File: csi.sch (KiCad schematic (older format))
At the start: 35 parts, among them J6 WE_68715014522, J7 WE_68715014022, U4 PCA9547BS,118

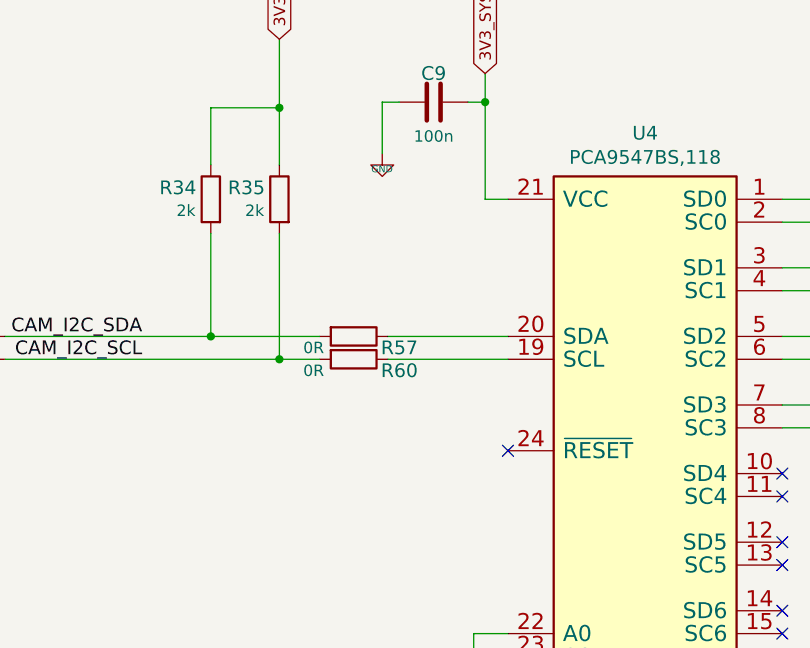
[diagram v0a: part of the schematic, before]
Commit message: Add i2c-mux reset pull-up
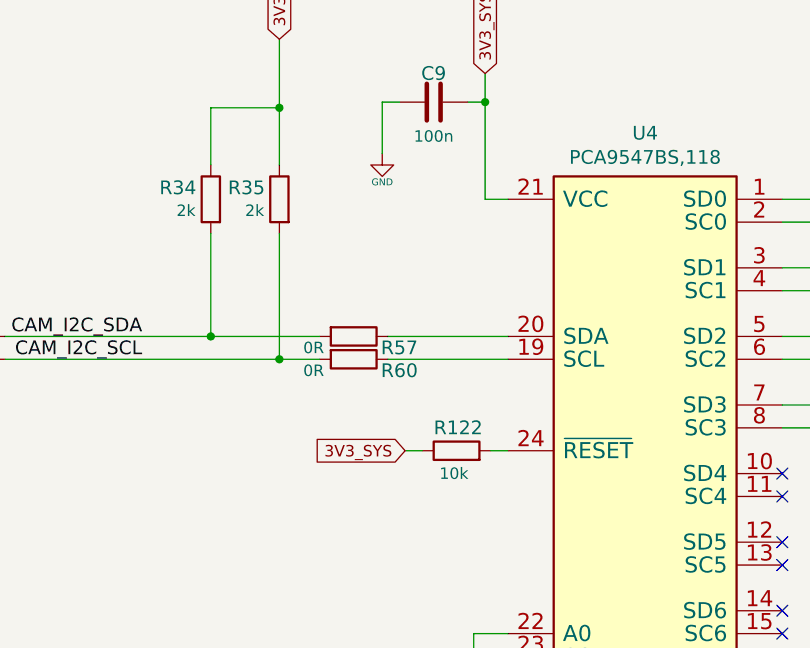
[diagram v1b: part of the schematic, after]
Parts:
- added R122: R_10k_0402, jetson-nano-baseboard-footprints:0402-res, symbol jetson-nano-baseboard:R_10k_0402
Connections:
- net 3V3_SYS: now also R122.1
- net at U4.24 (~RESET): now also R122.2
- no-connect marks 43 -> 42
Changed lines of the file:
@@
 AR Path="/60A05943/5E710510" Ref="#GND_?"  Part="1"
 F 0 "#GND_04" H 7300 8025 20  0001 C CNN
-F 1 "GND" H 7301 7957 30  0000 C CNN
+F 1 "GND" H 7300 7900 30  0000 C CNN
 F 2 "" H 7300 8025 70  0001 C CNN
 F 3 "" H 7300 8025 70  0001 C CNN
@@
 NoConn ~ 9050 10325
 NoConn ~ 9050 10425
-NoConn ~ 7850 9325
 Wire Wire Line
 	5650 8925 6850 8925
@@
 Wire Wire Line
 	6850 8925 7025 8925
+$Comp
+L jetson-nano-baseboard:R_10k_0402 R?
+U 1 1 6256B53A
+P 7625 9325
+AR Path="/608DF3E5/6256B53A" Ref="R?"  Part="1"
+AR Path="/60D9F63D/6256B53A" Ref="R122"  Part="1"
+F 0 "R122" H 7525 9425 60  0000 L CNN
+F 1 "R_10k_0402" H 7625 9175 60  0001 C CNN
+F 2 "jetson-nano-baseboard-footprints:0402-res" H 7825 9525 60  0001 L CNN
+F 3 "" H 7625 9325 50  0001 C CNN
+F 4 "VISHAY" H 7825 9725 60  0001 L CNN "Manufacturer"
+F 5 "CRCW040210K0FKEDHP" H 7825 9625 60  0001 L CNN "MPN"
+F 6 "10k" H 7550 9225 50  0000 L CNN "Val"
+	1    7625 9325
+	1    0    0    -1
+$EndComp
+Text GLabel 7400 9325 0    50   Input ~ 0
+3V3_SYS
+Wire Wire Line
+	7400 9325 7475 9325
+Wire Wire Line
+	7775 9325 7850 9325
 $EndSCHEMATC
